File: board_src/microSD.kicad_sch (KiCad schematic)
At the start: 2 parts, among them IC4 LM317T, J12 112J-TDAR-R01

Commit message: wersja dodane arkusze hierarchiczne
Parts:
- added D14: 1N4007, Diode_THT:D_DO-41_SOD81_P10.16mm_Horizontal, symbol Diode:1N4007
- added J14: Conn_01x07, symbol Connector_Generic:Conn_01x07
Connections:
- net m1: now reaches J12.1 (DAT2)
- net m1: now also J14.1 (Pin_1)
- net m2: now reaches J12.2 (CD/DAT3)
- net m2: now also J14.2 (Pin_2)
- net m3: now reaches J12.3 (CMD)
- net m3: now also J14.3 (Pin_3)
- net m4: now reaches J12.5 (CLK)
- net m4: now also J14.4 (Pin_4)
- net m5: now reaches J12.7 (DAT0)
- net m5: now also J14.5 (Pin_5)
- net m6: now reaches J12.8 (DAT1)
- net m6: now also J14.6 (Pin_6)
- net m7: now reaches J12.CD1 (CARD_DETECTION)
- net m7: now also J14.7 (Pin_7)
- net at IC4.2 (OUTPUT): now also D14.2 (A)
- net +7.0V: now reaches IC4.3 (INPUT)
- net +7.0V: now also D14.1 (K)
- net 3,3V renamed +3.3V
- net gnd renamed GND
- no-connect marks 0 -> 1
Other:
- note removed: "GPIO mikrokontrolera"
- note removed: "SPI"

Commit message: wersja uzupelnione footprinty
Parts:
- IC4: footprint TO255P460X1020X2008-3P -> footprints:TO255P460X1020X2008-3P
- J12: footprint 112JTDARR01 -> footprints:112JTDARR01
- J14: footprint (none) -> Connector_PinHeader_2.54mm:PinHeader_1x07_P2.54mm_Vertical
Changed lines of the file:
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@@
 			)
 		)
-		(property "Footprint" "112JTDARR01"
+		(property "Footprint" "footprints:112JTDARR01"
 			(at 143.51 188.9 0)
 			(effects
@@
 			)
 		)
-		(property "Footprint" "TO255P460X1020X2008-3P"
+		(property "Footprint" "footprints:TO255P460X1020X2008-3P"
 			(at 223.52 192.71 0)
 			(effects
@@
 			)
 		)
-		(property "Footprint" ""
+		(property "Footprint" "Connector_PinHeader_2.54mm:PinHeader_1x07_P2.54mm_Vertical"
 			(at 115.57 72.39 0)
 			(effects

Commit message: wersja 3d
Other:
- note added: "zmienić na nieregulowany"
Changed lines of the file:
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@@
+		)
+	)
+	(text "zmienić na nieregulowany"
+		(exclude_from_sim no)
+		(at 224.536 111.506 0)
+		(effects
+			(font
+				(size 1.27 1.27)
+			)
 		)
 	)

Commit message: uporzadkowane 3D
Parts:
- removed D14: 1N4007, Diode_THT:D_DO-41_SOD81_P10.16mm_Horizontal, symbol Diode:1N4007
- removed IC4: LM317T, footprints:TO255P460X1020X2008-3P, symbol LM317T:LM317T
- added C3, C7: 10uF, symbol Device:C_Small
- added C5, C6: 100uF, symbol Device:C_Small
- added PS1: AP2202K-3.3TRG1, footprints:SOT95P282X145-5N, symbol AP2202K-3_3TRG1:AP2202K-3.3TRG1
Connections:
- net +3.3V: now also C7.2, PS1.5 (VOUT)
- net GND: now also C5.1, C6.1, PS1.2 (GND)
- new net: C3.1, C5.2
- new net: C6.2, C7.1
- new net +5.0V: C3.2, PS1.1 (VIN), PS1.3 (EN)
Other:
- note removed: "stabilizator napięcia"
- note removed: "zmienić na nieregulowany"

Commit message: wersja z wyswietlaczem LCD
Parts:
- C3, C5, C6, C7: footprint (none) -> Capacitor_SMD:C_0201_0603Metric
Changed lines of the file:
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@@
 			)
 		)
-		(property "Footprint" ""
+		(property "Footprint" "Capacitor_SMD:C_0201_0603Metric"
 			(at 123.19 132.08 0)
 			(effects
@@
 			)
 		)
-		(property "Footprint" ""
+		(property "Footprint" "Capacitor_SMD:C_0201_0603Metric"
 			(at 115.57 132.08 0)
 			(effects
@@
 			)
 		)
-		(property "Footprint" ""
+		(property "Footprint" "Capacitor_SMD:C_0201_0603Metric"
 			(at 154.94 142.24 0)
 			(effects
@@
 			)
 		)
-		(property "Footprint" ""
+		(property "Footprint" "Capacitor_SMD:C_0201_0603Metric"
 			(at 162.56 142.24 0)
 			(effects

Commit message: wersja z FT232RN
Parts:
- removed C3, C7: 10uF, Capacitor_SMD:C_0201_0603Metric, symbol Device:C_Small
- removed C5, C6: 100uF, Capacitor_SMD:C_0201_0603Metric, symbol Device:C_Small
- removed PS1: AP2202K-3.3TRG1, footprints:SOT95P282X145-5N, symbol AP2202K-3_3TRG1:AP2202K-3.3TRG1
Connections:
- net +3.3V: now also J12.6 (VSS)
- net GND: no longer J12.6 (VSS)
- no-connect marks 1 -> 0

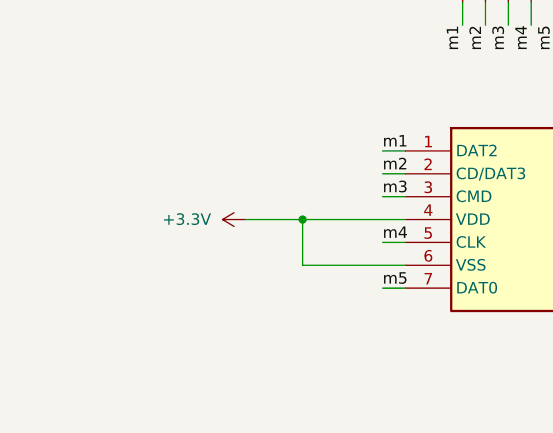
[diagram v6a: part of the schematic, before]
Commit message: Wersja ze sciezkami miedzianymi
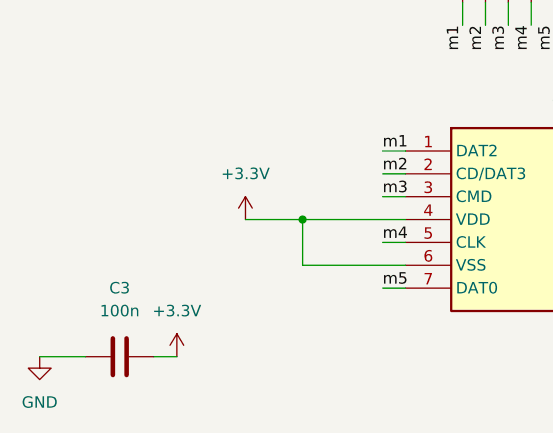
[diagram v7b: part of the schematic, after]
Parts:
- added C3: 100n, Capacitor_SMD:C_0603_1608Metric, symbol Device:C
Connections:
- net +3.3V: now also C3.2
- net GND: now also C3.1
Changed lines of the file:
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@@
+	(wire
+		(pts
+			(xy 60.96 116.84) (xy 66.04 116.84)
+		)
+		(stroke
+			(width 0)
+			(type default)
+		)
+	)
 	(wire
 		(pts
@@
 		(pts
 			(xy 120.65 77.47) (xy 120.65 80.01)
+		)
+		(stroke
+			(width 0)
+			(type default)
+		)
+	)
+	(wire
+		(pts
+			(xy 73.66 116.84) (xy 76.2 116.84)
 		)
 		(stroke
@@
 	(symbol
 		(lib_id "power:+3.3V")
-		(at 83.82 101.6 90)
+		(at 83.82 101.6 0)
 		(unit 1)
 		(exclude_from_sim no)
@@
 		(fields_autoplaced yes)
 		(property "Reference" "#PWR012"
-			(at 87.63 101.6 0)
+			(at 83.82 105.41 0)
 			(effects
 				(font
@@
 		)
 		(property "Value" "+3.3V"
-			(at 80.01 101.5999 90)
-			(effects
-				(font
-					(size 1.27 1.27)
-				)
-				(justify left)
+			(at 83.82 96.52 0)
+			(effects
+				(font
+					(size 1.27 1.27)
+				)
 			)
 		)
@@
 					(unit 1)
 				)
+			)
+		)
+	)
+	(symbol
+		(lib_id "Device:C")
+		(at 69.85 116.84 90)
+		(unit 1)
+		(exclude_from_sim no)
+		(in_bom yes)
+		(on_board yes)
+		(dnp no)
+		(fields_autoplaced yes)
+		(property "Reference" "C3"
+			(at 69.85 109.22 90)
+			(effects
+				(font
+					(size 1.27 1.27)
+				)
+			)
+		)
+		(property "Value" "100n"
+			(at 69.85 111.76 90)
+			(effects
+				(font
+					(size 1.27 1.27)
+				)
+			)
+		)
+		(property "Footprint" "Capacitor_SMD:C_0603_1608Metric"
+			(at 73.66 115.8748 0)
+			(effects
+				(font
+					(size 1.27 1.27)
+				)
+				(hide yes)
+			)
+		)
+		(property "Datasheet" "~"
+			(at 69.85 116.84 0)
+			(effects
+				(font
+					(size 1.27 1.27)
+				)
+				(hide yes)
+			)
+		)
+		(property "Description" "Unpolarized capacitor"
+			(at 69.85 116.84 0)
+			(effects
+				(font
+					(size 1.27 1.27)
+				)
+				(hide yes)
+			)
+		)
+		(pin "2"
+		)
+		(pin "1"
+		)
+		(instances
+			(project "board"
+				(path "/772e9f49-cfcf-4cf6-843d-0684684f2d4b/7bb65ccf-4598-4b69-a1c1-81fe3a474d8e"
+					(reference "C3")
+					(unit 1)
+				)
+			)
+		)
+	)
+	(symbol
+		(lib_id "power:GND")
+		(at 60.96 116.84 0)
+		(unit 1)
+		(exclude_from_sim no)
+		(in_bom yes)
+		(on_board yes)
+		(dnp no)
+		(fields_autoplaced yes)
+		(property "Reference" "#PWR025"
+			(at 60.96 123.19 0)
+			(effects
+				(font
+					(size 1.27 1.27)
+				)
+				(hide yes)
+			)
+		)
+		(property "Value" "GND"
+			(at 60.96 121.92 0)
+			(effects
+				(font
+					(size 1.27 1.27)
+				)
+			)
+		)
+		(property "Footprint" ""
+			(at 60.96 116.84 0)
+			(effects
+				(font
+					(size 1.27 1.27)
+				)
+				(hide yes)
+			)
+		)
+		(property "Datasheet" ""
+			(at 60.96 116.84 0)
+			(effects
+				(font
+					(size 1.27 1.27)
+				)
+				(hide yes)
+			)
+		)
+		(property "Description" "Power symbol creates a global label with name \"GND\" , ground"
+			(at 60.96 116.84 0)
+			(effects
+				(font
+					(size 1.27 1.27)
+				)
+				(hide yes)
+			)
+		)
+		(pin "1"
+		)
+		(instances
+			(project "board"
+				(path "/772e9f49-cfcf-4cf6-843d-0684684f2d4b/7bb65ccf-4598-4b69-a1c1-81fe3a474d8e"
+					(reference "#PWR025")
+					(unit 1)
+				)
+			)
+		)
+	)
+	(symbol
+		(lib_id "power:+3.3V")
+		(at 76.2 116.84 0)
+		(unit 1)
+		(exclude_from_sim no)
+		(in_bom yes)
+		(on_board yes)
+		(dnp no)
+		(fields_autoplaced yes)
+		(property "Reference" "#PWR054"
+			(at 76.2 120.65 0)
+			(effects
+				(font
+					(size 1.27 1.27)
+				)
+				(hide yes)
+			)
+		)
+		(property "Value" "+3.3V"
+			(at 76.2 111.76 0)
+			(effects
+				(font
+					(size 1.27 1.27)
+				)
+			)
+		)
+		(property "Footprint" ""
+			(at 76.2 116.84 0)
+			(effects
+				(font
+					(size 1.27 1.27)
+				)
+				(hide yes)
+			)
+		)
+		(property "Datasheet" ""
+			(at 76.2 116.84 0)
+			(effects
+				(font
+					(size 1.27 1.27)
+				)
+				(hide yes)
+			)
+		)
+		(property "Description" "Power symbol creates a global label with name \"+3.3V\""
+			(at 76.2 116.84 0)
+			(effects
+				(font
+					(size 1.27 1.27)
+				)
+				(hide yes)
+			)
+		)
+		(pin "1"
+		)
+		(instances
+			(project "board"
+				(path "/772e9f49-cfcf-4cf6-843d-0684684f2d4b/7bb65ccf-4598-4b69-a1c1-81fe3a474d8e"
+					(reference "#PWR054")
+					(unit 1)
+				)

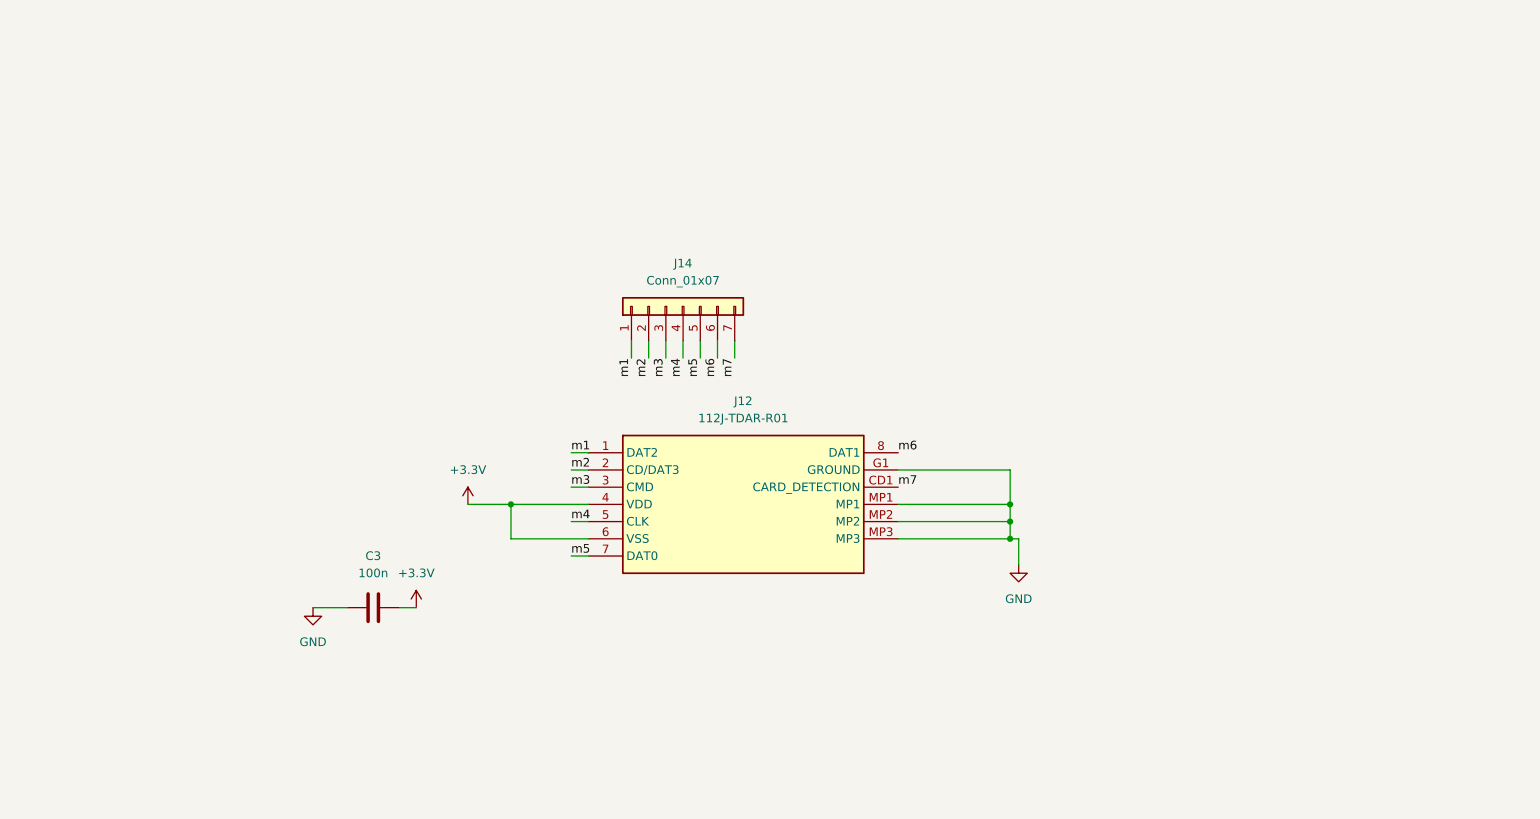
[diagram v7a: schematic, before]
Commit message: Poprawki w schematach. Rozpoczęte korekty płytki
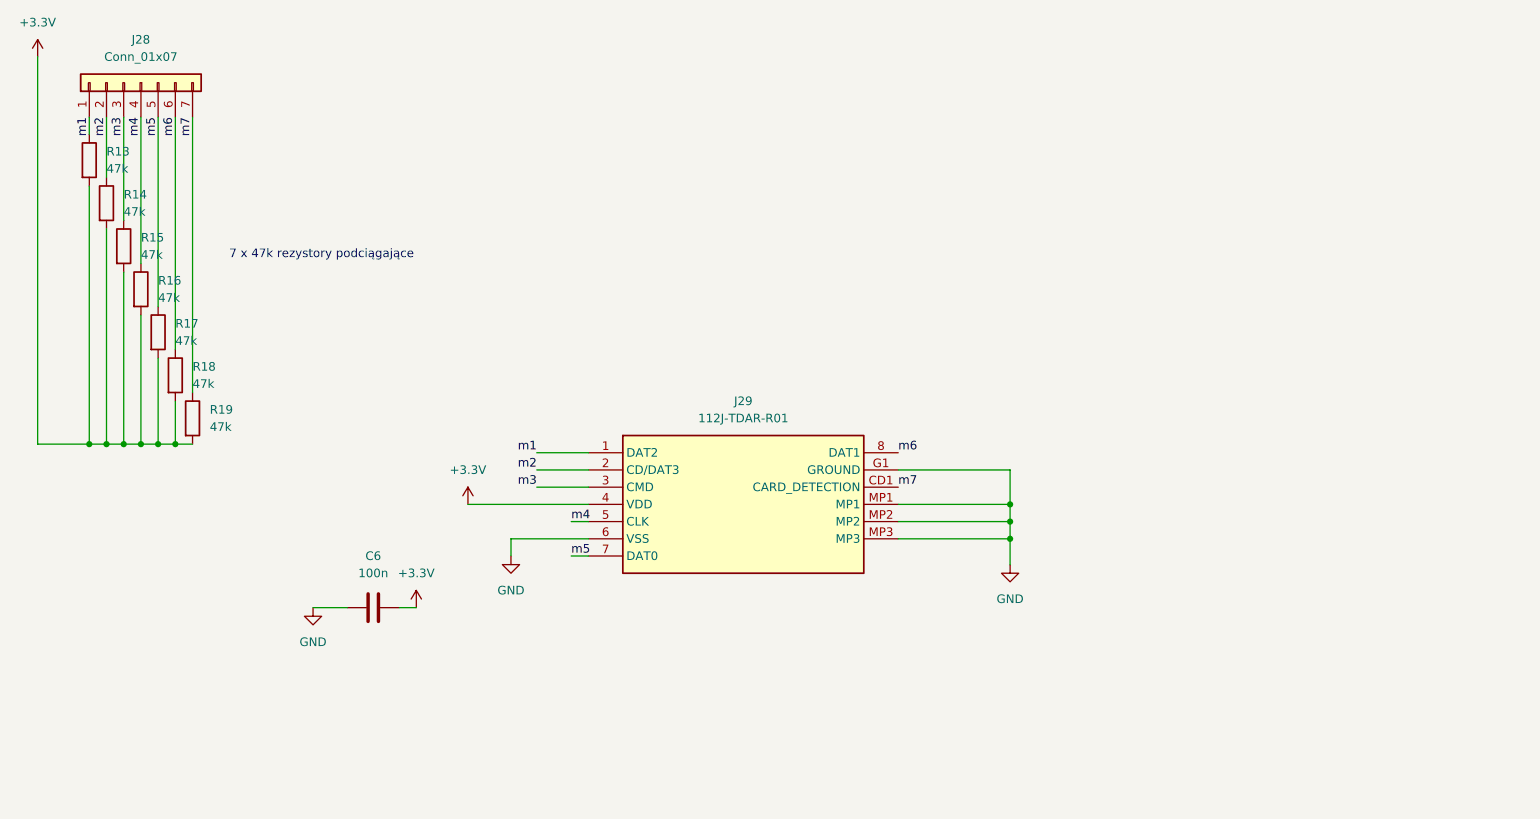
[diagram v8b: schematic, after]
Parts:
- added R13, R14, R15, R16, R17, R18, R19: 47k, Resistor_SMD:R_0603_1608Metric_Pad0.98x0.95mm_HandSolder, symbol Device:R
- C6: renamed from C3; footprint Capacitor_SMD:C_0603_1608Metric -> Capacitor_SMD:C_0603_1608Metric_Pad1.08x0.95mm_HandSolder
- J28: renamed from J14; footprint Connector_PinHeader_2.54mm:PinHeader_1x07_P2.54mm_Vertical -> Connector_PinHeader_2.54mm:PinHeader_1x04_P2.54mm_Vertical
- J29: renamed from J12; footprint footprints:112JTDARR01 -> Connector_PinHeader_2.54mm:PinHeader_1x08_P2.54mm_Vertical
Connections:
- net +3.3V: now also R13.2, R14.2, R15.2, R16.2, R17.2, R18.2, R19.2; no longer J29.6 (VSS)
- net GND: now also J29.6 (VSS)
- net m1: now also R13.1
- net m2: now also R14.1
- net m3: now also R15.1
- net m4: now also R16.1
- net m5: now also R17.1
- net m6: now also R18.1
- net m7: now also R19.1
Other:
- note added: "7 x 47k rezystory podciągające"
- moved on the sheet: J28
